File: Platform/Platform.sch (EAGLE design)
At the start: 35 parts, among them U1 FT232RLSSOP, X1 USBSMD, Y1 RESONATORSMD

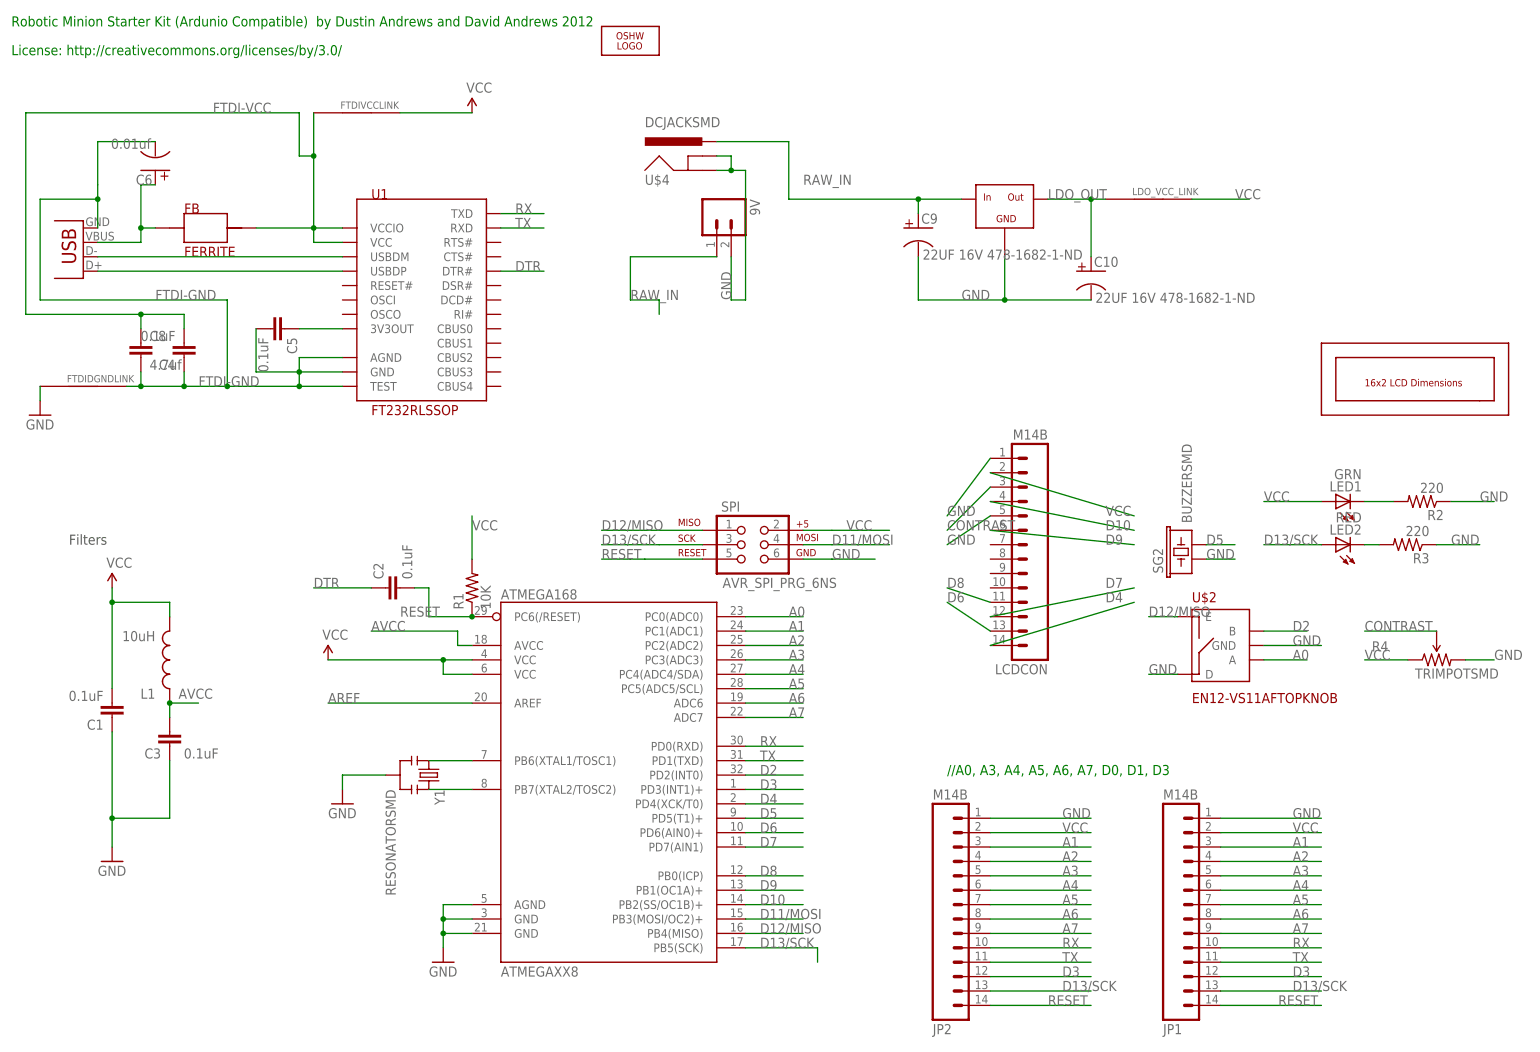
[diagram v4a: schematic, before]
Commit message: Better filter placement and moved 9v terminal to a better spot
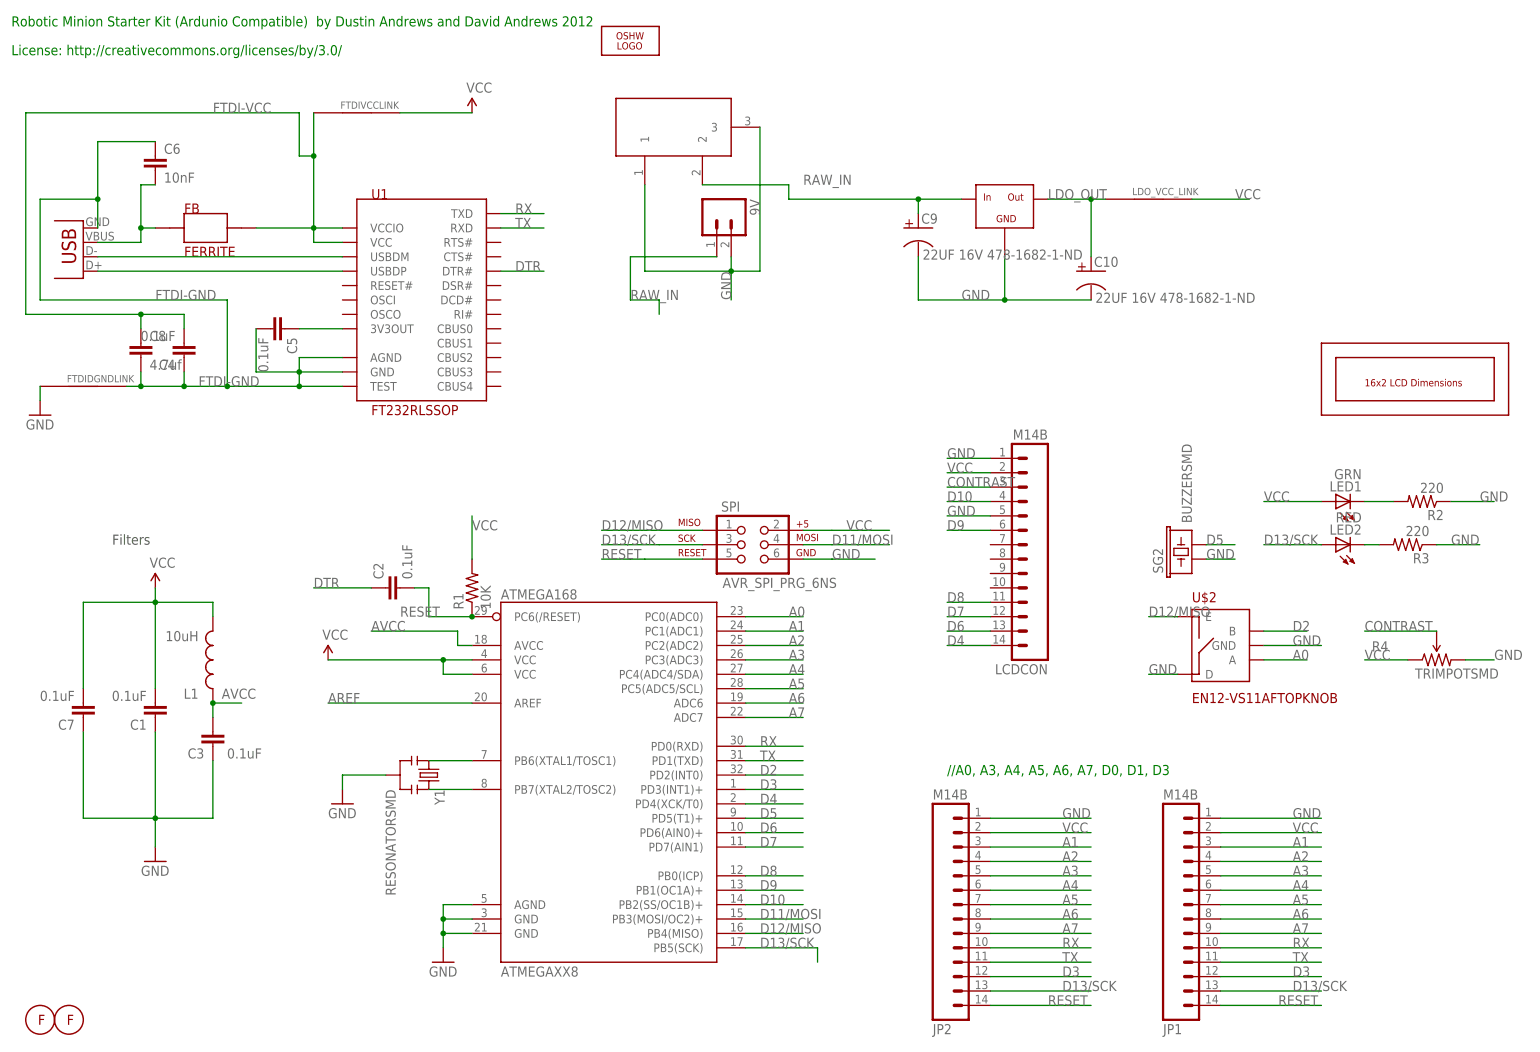
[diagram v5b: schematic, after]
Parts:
- removed U$4: DCJACKSMD, Dustin:DCJACKSMD
- added C7: 0.1uF, SparkFun:CAP0805
- added FM1, FM2: FIDUCIAL1MM, ads4:FIDUCIAL1MM
- added J1: DC21MMX, powersupply:DC21MMX
- C6: value 0.01uf -> 10nF; device Dustin:CAP_POL -> rcl:C-EUC0805; DIGIKEY# 478-1383-1-ND -> (none)
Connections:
- net FTDI-GND: now also C6.1; no longer C6.-
- net GND: now also C7.1, J1.1, J1.3; no longer U$4.GND, U$4.GNDBREAK
- net RAW_IN: now also J1.2; no longer U$4.PWR
- net VBUS: now also C6.2; no longer C6.+
- net VCC: now also C7.2
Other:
- moved on the sheet: C1, C3, L1

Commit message: Final Design for Production
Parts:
- renumbered FB to GND
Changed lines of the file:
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@@
 <?xml version="1.0" encoding="utf-8"?>
 <!DOCTYPE eagle SYSTEM "eagle.dtd">
-<eagle version="6.2">
+<eagle version="6.1">
 <drawing>
 <settings>
@@
 <attribute name="DIGIKEY#" value="768-1007-1-ND"/>
 </part>
-<part name="FB" library="Dustin" deviceset="FERRITE" device="">
+<part name="GND" library="Dustin" deviceset="FERRITE" device="">
 <attribute name="DIGIKEY#" value="240-2399-1-ND"/>
 </part>
@@
 <attribute name="DIGIKEY#" x="66.04" y="134.62" size="1.778" layer="96" display="off"/>
 </instance>
-<instance part="FB" gate="G$1" x="27.94" y="149.86">
+<instance part="GND" gate="G$1" x="27.94" y="149.86">
 <attribute name="DIGIKEY#" x="27.94" y="149.86" size="1.778" layer="96" display="off"/>
 </instance>
@@
 <wire x1="10.16" y1="147.32" x2="17.78" y2="147.32" width="0.1524" layer="91"/>
 <wire x1="17.78" y1="147.32" x2="17.78" y2="149.86" width="0.1524" layer="91"/>
-<pinref part="FB" gate="G$1" pin="P$1"/>
+<pinref part="GND" gate="G$1" pin="P$1"/>
 <wire x1="17.78" y1="149.86" x2="20.32" y2="149.86" width="0.1524" layer="91"/>
 <junction x="17.78" y="149.86"/>
@@
 <net name="FTDI-VCC" class="0">
 <segment>
-<pinref part="FB" gate="G$1" pin="P$2"/>
+<pinref part="GND" gate="G$1" pin="P$2"/>
 <wire x1="38.1" y1="149.86" x2="48.26" y2="149.86" width="0.1524" layer="91"/>
 <junction x="48.26" y="149.86"/>
